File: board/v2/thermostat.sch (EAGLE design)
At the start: 18 parts, among them IC1 7805TV, Q1 MOSFET-NCHANNEL2N7000, Q2 MOSFET-NCHANNEL2N7000, Q3 MOSFET-NCHANNEL2N7000

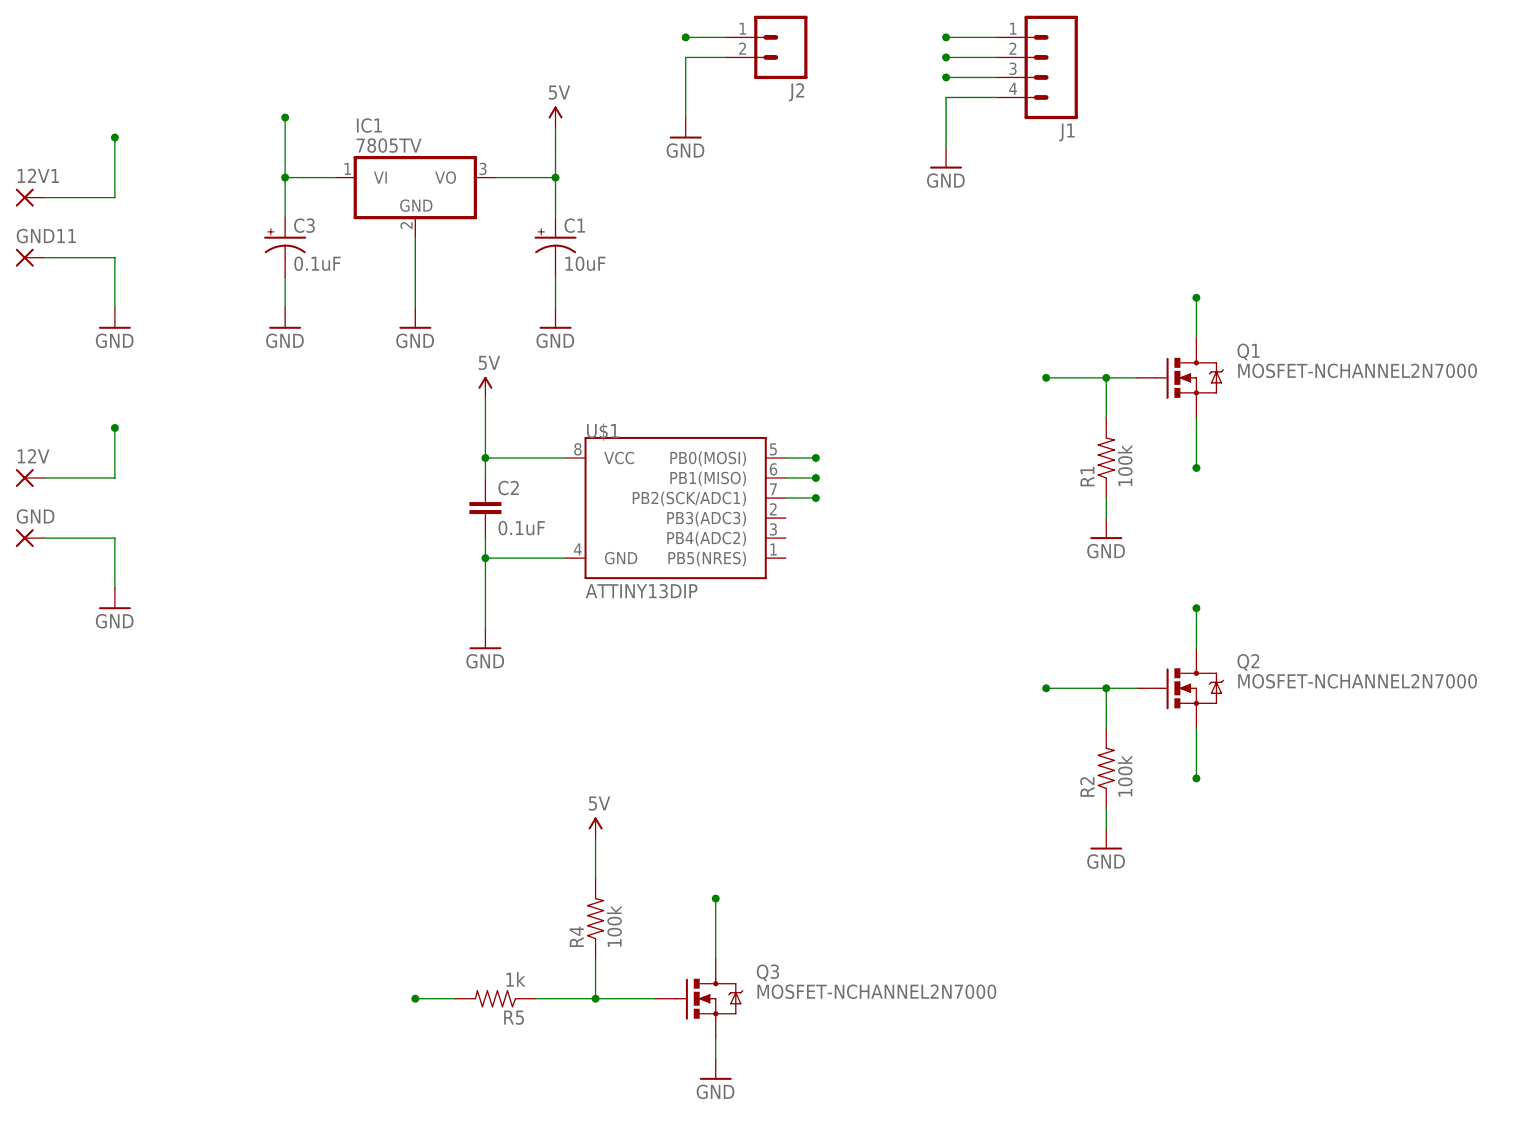
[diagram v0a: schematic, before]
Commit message: SMD layout complete
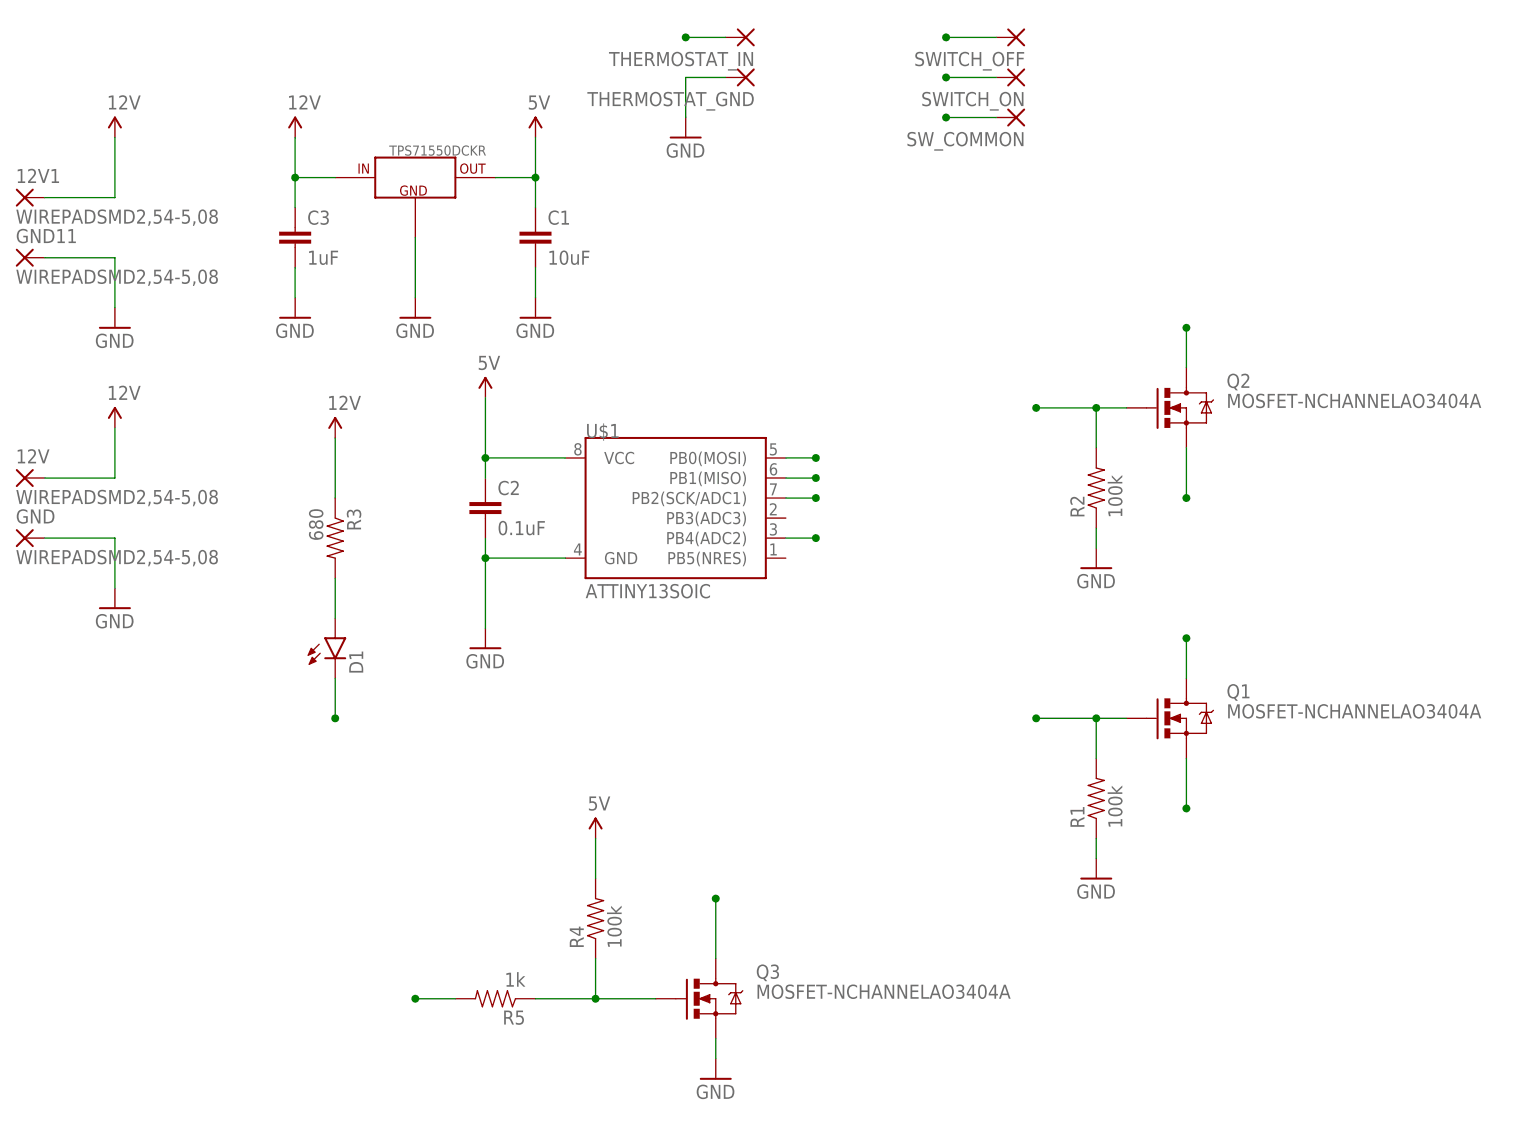
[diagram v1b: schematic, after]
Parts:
- removed IC1: 7805TV, linear:7805TV
- removed J1: (no value), SparkFun-Connectors:M04PTH
- removed J2: (no value), SparkFun-Connectors:M02PTH
- added D1: (no value), SparkFun-LED:LED0603
- added R3: 680, SparkFun-Passives:RESISTOR0805-RES
- added SWITCH_OFF, SWITCH_ON, SW_COMMON, THERMOSTAT_GND, THERMOSTAT_IN: WIREPADSMD2,54-5,08, wirepad:WIREPADSMD2,54-5,08
- added TPS71550DCKR: (no value), Synapseware:TPS715XX
- 12V, 12V1, GND, GND11: value WIREPAD2,54/0,8 -> WIREPADSMD2,54-5,08; device wirepad:WIREPAD2,54/0,8 -> wirepad:WIREPADSMD2,54-5,08
- C1: device SparkFun-Capacitors:CAP_POLPTH2 -> SparkFun-Capacitors:CAP1210
- C2: device SparkFun-Capacitors:CAPEZ -> SparkFun-Capacitors:CAP0805
- C3: value 0.1uF -> 1uF; device SparkFun-Capacitors:CAP_POLPTH2 -> SparkFun-Capacitors:CAP1210
- Q1, Q2, Q3: value MOSFET-NCHANNEL2N7000 -> MOSFET-NCHANNELAO3404A; device SparkFun-DiscreteSemi:MOSFET-NCHANNEL2N7000 -> SparkFun-DiscreteSemi:MOSFET-NCHANNELAO3404A
- R1, R2, R4, R5: device SparkFun-Passives:RESISTORAXIAL-0.3 -> SparkFun-Passives:RESISTOR0805-RES
- U$1: value ATTINY13DIP -> ATTINY13SOIC; device SparkFun-DigitalIC:ATTINY13DIP -> SparkFun-DigitalIC:ATTINY13SOIC
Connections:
- new net LED: D1.C, U$1.PB4(ADC2)
- new net N$2: D1.A, R3.2
- net 12V: now also C3.1, R3.1, TPS71550DCKR.IN; no longer C3.+, IC1.VI
- net 5V: now also C1.1, TPS71550DCKR.OUT; no longer C1.+, IC1.VO
- net GND: now also C1.2, C3.2, THERMOSTAT_GND.P, TPS71550DCKR.GND; no longer C1.-, C3.-, IC1.GND, J1.4, J2.2
- net SWITCH_OFF: now also SWITCH_OFF.P; no longer J1.1
- net SWITCH_ON: now also SWITCH_ON.P; no longer J1.2
- net SW_COMMON: now also SW_COMMON.P; no longer J1.3
- net THERMOSTAT_IN: now also THERMOSTAT_IN.P; no longer J2.1
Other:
- moved on the sheet: Q1, Q2, R1, R2
